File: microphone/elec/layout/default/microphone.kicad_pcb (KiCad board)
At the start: 2 copper layers, 225.7 x 100.8 mm, 0 parts

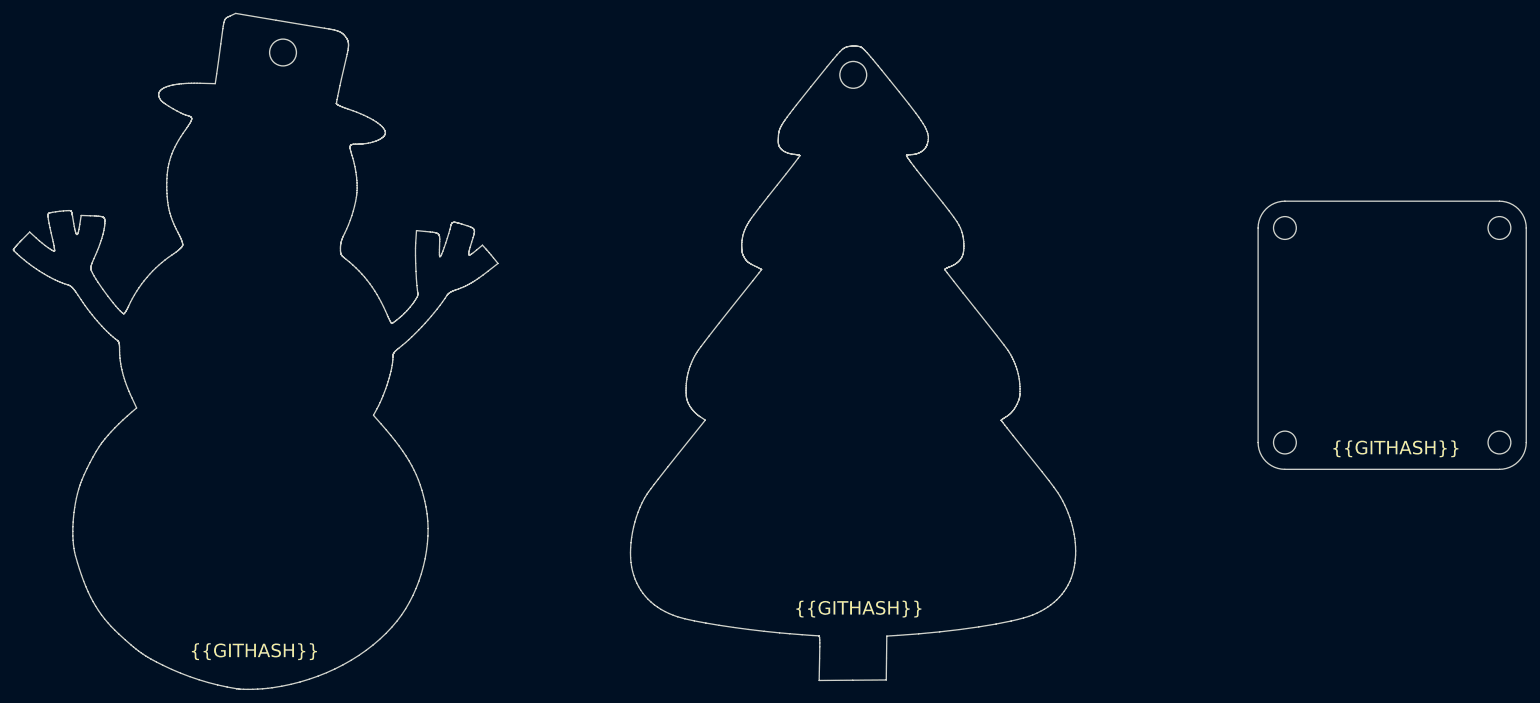
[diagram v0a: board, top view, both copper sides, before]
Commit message: replaced microphone model with one that is available and from well known company
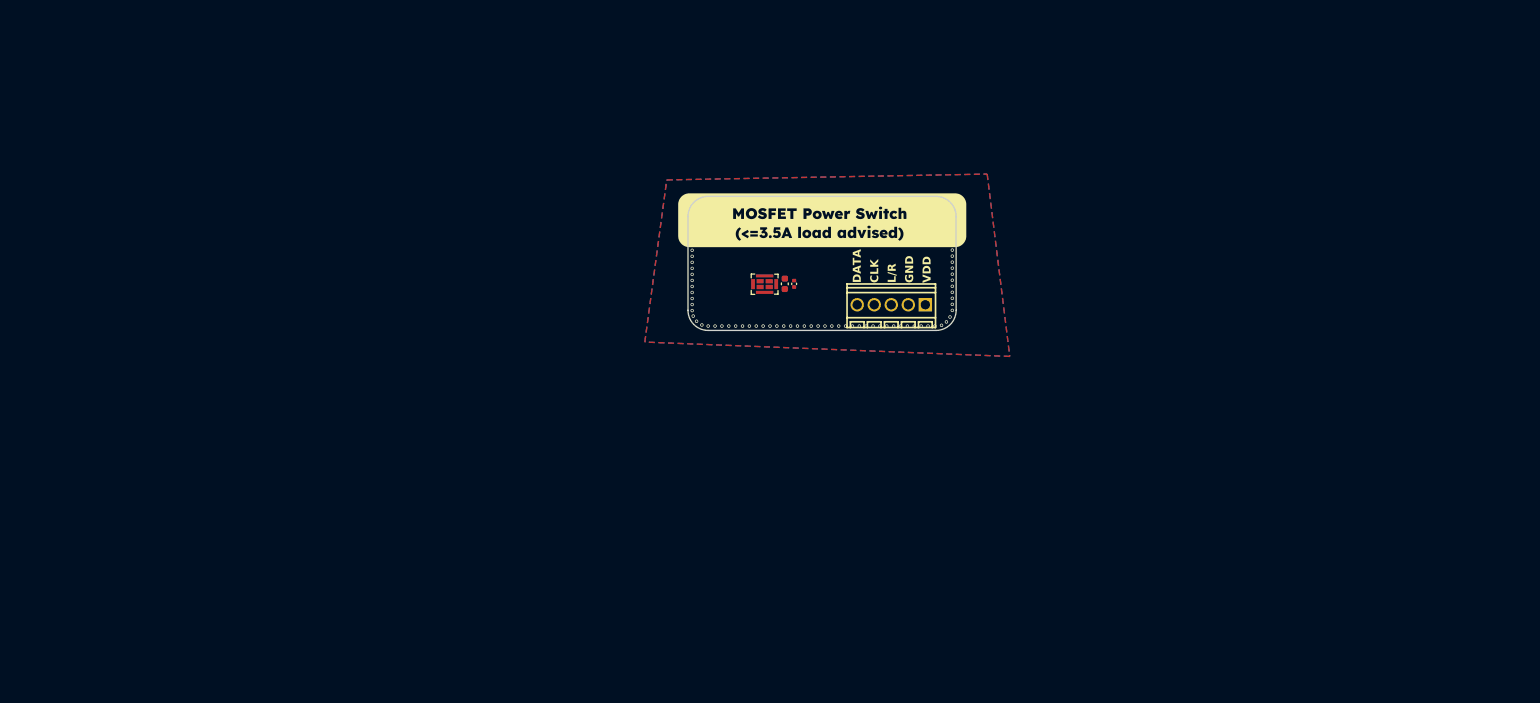
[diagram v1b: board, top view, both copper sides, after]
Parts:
- added C1: 25V 10uF X5R ±20% 0603 Multilayer Ceramic Capacitors MLCC -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, lib:C0603, F.Cu at (151.0, 90.1)
- added C2: 16V 100nF X7R ±10% 0402 Multilayer Ceramic Capacitors MLCC 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, lib:C0402, F.Cu at (152.4, 90.1)
- added U1: , lib:MIC-SMD_8P-L4.0-W3.0_ZTS6231, F.Cu at (148.0, 90.2)
- added U2: , lib:CONN-TH_XY308-2.54-5P, F.Cu at (166.9, 93.2)
- added U3: , lib:MountingHole_3.2mm_M3, F.Cu at (172.3, 81.3)
- added U4: , lib:MountingHole_3.2mm_M3, F.Cu at (140.8, 81.3)
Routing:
- net gnd: vias 0 -> 144
- added copper zone on B.Cu, net gnd
- added copper zone on F.Cu, net gnd
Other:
- board size 225.7 x 100.8 mm -> 40 x 20 mm
- board text added: "CLK"
- board text added: "DATA"
- board text added: "GND"
- board text added: "L/R"
- board text added: "Source files:"
- board text added: "VDD"
- board text added: "bit.ly/..."
- board text added: "designed by glowingkitty"
